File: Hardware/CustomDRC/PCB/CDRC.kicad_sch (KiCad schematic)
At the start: 1 part, among them J101 DSP Header

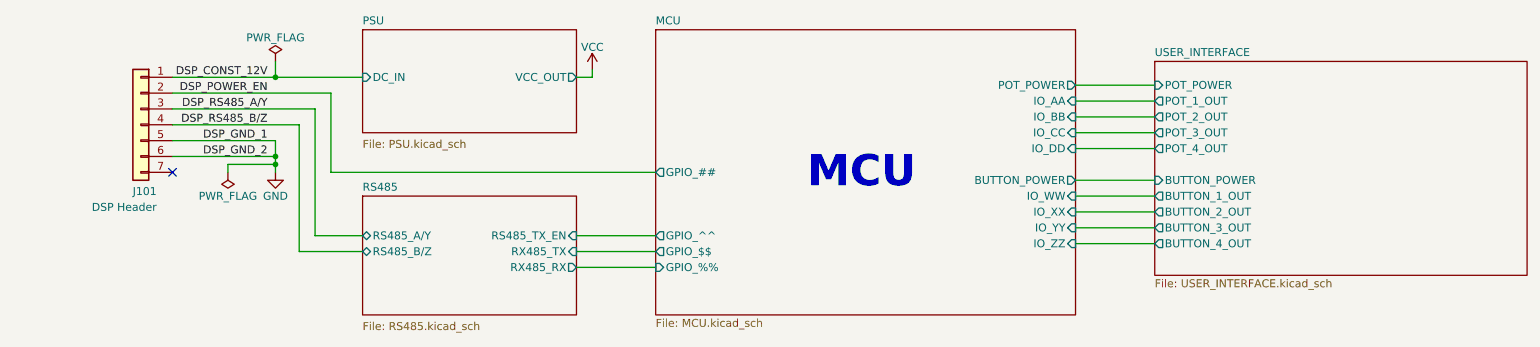
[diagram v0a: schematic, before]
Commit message: Update - Schematics
Added new reverse engineered schematic. Also updated main PCB folder structure
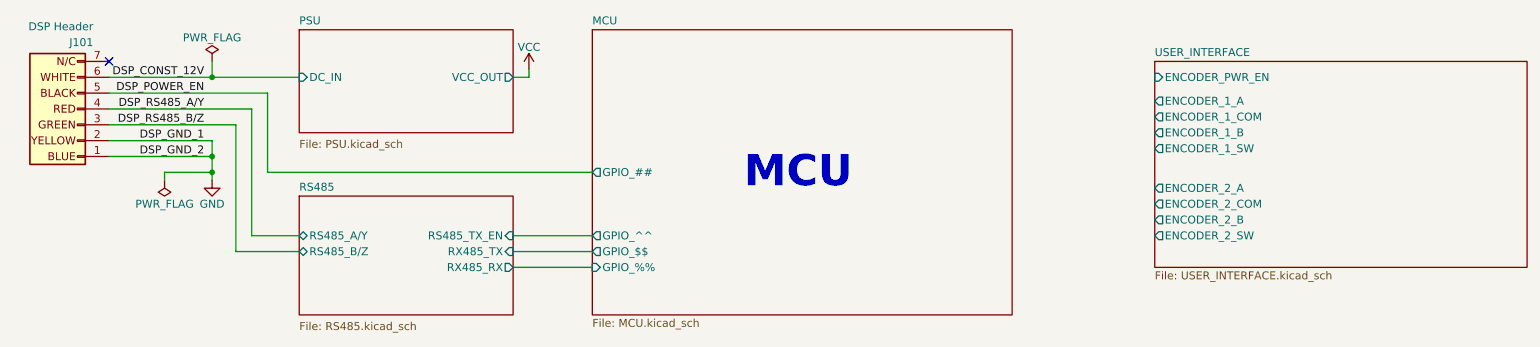
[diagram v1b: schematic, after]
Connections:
- net DSP_CONST_12V: now also J101.6 (Pin_6); no longer J101.1 (Pin_1)
- net DSP_POWER_EN: now also J101.5 (Pin_5); no longer J101.2 (Pin_2)
- net DSP_RS485_A/Y: now also J101.4 (Pin_4); no longer J101.3 (Pin_3)
- net DSP_RS485_B/Z: now also J101.3 (Pin_3); no longer J101.4 (Pin_4)
- net GND: now also J101.1 (Pin_1), J101.2 (Pin_2); no longer J101.5 (Pin_5), J101.6 (Pin_6)
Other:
- sheet MCU ports: added none; removed BUTTON_POWER, IO_AA, IO_BB, IO_CC, IO_DD, IO_WW, IO_XX, IO_YY, IO_ZZ, POT_POWER
- sheet USER_INTERFACE ports: added ENCODER_1_A, ENCODER_1_B, ENCODER_1_COM, ENCODER_1_SW, ENCODER_2_A, ENCODER_2_B, ENCODER_2_COM, ENCODER_2_SW, ENCODER_PWR_EN; removed BUTTON_1_OUT, BUTTON_2_OUT, BUTTON_3_OUT, BUTTON_4_OUT, BUTTON_POWER, POT_1_OUT, POT_2_OUT, POT_3_OUT, POT_4_OUT, POT_POWER

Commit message: Update - finished schematic for revision A
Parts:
- added H101, H102, H103: MountingHole, MountingHole:MountingHole_2.7mm_M2.5, symbol Mechanical:MountingHole
- added TP101: TestPoint_Small, TestPoint:TestPoint_Keystone_5000-5004_Miniature, symbol Connector:TestPoint_Small
- added TP102, TP103: TestPoint_Small, TestPoint:TestPoint_Pad_D1.5mm, symbol Connector:TestPoint_Small
- J101: LCSC (none) -> C18905866; MPN (none) -> XDZ254-1-06-W-2.5-G1; Manufacturer (none) -> chxunda
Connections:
- net DSP_CONST_12V: now also J101.7 (Pin_7), TP102.1; no longer J101.6 (Pin_6)
- net DSP_POWER_EN: now also J101.6 (Pin_6), TP103.1; no longer J101.5 (Pin_5)
- net DSP_RS485_A/Y: now also J101.5 (Pin_5); no longer J101.4 (Pin_4)
- net DSP_RS485_B/Z: now also J101.4 (Pin_4); no longer J101.3 (Pin_3)
- net GND: now also J101.3 (Pin_3), TP101.1; no longer J101.1 (Pin_1)
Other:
- sheet MCU ports: added GPIO36, GPIO39, IO18, IO19, IO21, IO25, IO32, IO33, IO34, IO35, IO5; removed GPIO_##, GPIO_$$, GPIO_%%, GPIO_^^
- sheet PSU ports: added none; removed VCC_OUT
- sheet RS485 ports: added RS485_RX, RS485_TX; removed RX485_RX, RX485_TX
- sheet USER_INTERFACE ports: added LED_PWM; removed ENCODER_1_COM, ENCODER_2_COM, ENCODER_PWR_EN
- moved on the sheet: J101

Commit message: Sync HW changes for V1 PCB
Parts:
- J101: LCSC C18905866 -> C7501615; MPN XDZ254-1-06-W-2.5-G1 -> PH2.54-07-06PWD; Manufacturer chxunda -> XUNPU
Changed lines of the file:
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@@
 	(title_block
 		(title "CDRC - Custom DRC for Audison AC Link")
-		(date "2024-08-20")
+		(date "03-09-2024")
 		(rev "A")
 		(company "JS HW")
@@
 			(width 0)
 			(type default)
+		)
+	)
+	(text_box "REVISION HISTORY:\n\nA: Initial design"
+		(exclude_from_sim no)
+		(at 177.546 139.7 0)
+		(size 101.6 20.828)
+		(stroke
+			(width 0)
+			(type default)
+		)
+		(fill
+			(type none)
+		)
+		(effects
+			(font
+				(size 2 2)
+				(thickness 0.4)
+				(bold yes)
+			)
+			(justify left top)
 		)
 	)
@@
 			)
 		)
-		(property "LCSC" " C18905866"
+		(property "LCSC" "C7501615"
 			(at 36.83 83.82 0)
 			(effects
@@
 			)
 		)
-		(property "Manufacturer" " chxunda"
+		(property "Manufacturer" "XUNPU"
 			(at 36.83 83.82 0)
 			(effects
@@
 			)
 		)
-		(property "MPN" "XDZ254-1-06-W-2.5-G1"
+		(property "MPN" "PH2.54-07-06PWD"
 			(at 36.83 83.82 0)
 			(effects

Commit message: Sync before making breaking changes to RS485 comms protocl and method
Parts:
- H101, H102, H103: footprint MountingHole:MountingHole_2.7mm_M2.5 -> MountingHole:MountingHole_2.7mm_M2.5_ISO7380_Pad_TopOnly
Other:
- sheet MCU ports: added IO27, IO36, IO39; removed GPIO36, GPIO39, IO21
- title: CDRC - Custom DRC for Audison AC Link -> CDRC - Custom DRC for Bit 10D
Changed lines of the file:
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@@
 	(paper "A4")
 	(title_block
-		(title "CDRC - Custom DRC for Audison AC Link")
-		(date "03-09-2024")
-		(rev "A")
+		(title "CDRC - Custom DRC for Bit 10D")
+		(date "01-11-2024")
+		(rev "B")
 		(company "JS HW")
 	)
@@
 		)
 	)
-	(text_box "REVISION HISTORY:\n\nA: Initial design"
+	(text_box "ISSUES:\n- DRC requires listenting to RS485 on sleep to wake-up when DSP is powered on.\n	Requires ESP32 to assign RX pin to an RTC power domain IO (IO27 will work)"
+		(exclude_from_sim no)
+		(at 18.796 164.338 0)
+		(size 101.092 28.702)
+		(stroke
+			(width 0)
+			(type default)
+		)
+		(fill
+			(type none)
+		)
+		(effects
+			(font
+				(size 1.27 1.27)
+				(thickness 0.254)
+				(bold yes)
+			)
+			(justify left top)
+		)
+	)
+	(text_box "REVISION HISTORY:\n\nA: Initial design\nB: Changed RS485 RX connection to ESP32 from GPIO21 to GPIO27	\nRemoved solder bridge pads to control RS485_RX_EN. Confirmed working as intended"
 		(exclude_from_sim no)
 		(at 177.546 139.7 0)
-		(size 101.6 20.828)
+		(size 101.6 24.892)
 		(stroke
 			(width 0)
@@
 			)
 		)
-		(property "Footprint" "MountingHole:MountingHole_2.7mm_M2.5"
+		(property "Footprint" "MountingHole:MountingHole_2.7mm_M2.5_ISO7380_Pad_TopOnly"
 			(at 96.52 135.89 0)
 			(effects
@@
 			)
 		)
-		(property "Footprint" "MountingHole:MountingHole_2.7mm_M2.5"
+		(property "Footprint" "MountingHole:MountingHole_2.7mm_M2.5_ISO7380_Pad_TopOnly"
 			(at 96.52 148.59 0)
 			(effects
@@
 			)
 		)
-		(property "Footprint" "MountingHole:MountingHole_2.7mm_M2.5"
+		(property "Footprint" "MountingHole:MountingHole_2.7mm_M2.5_ISO7380_Pad_TopOnly"
 			(at 96.52 142.24 0)
 			(effects
@@
 			)
 		)
-		(pin "GPIO39" input
-			(at 186.69 91.44 0)
-			(effects
-				(font
-					(size 1.27 1.27)
-				)
-				(justify right)
-			)
-		)
-		(pin "GPIO36" input
-			(at 186.69 88.9 0)
-			(effects
-				(font
-					(size 1.27 1.27)
-				)
-				(justify right)
-			)
-		)
 		(pin "IO19" bidirectional
 			(at 119.38 101.6 180)
@@
 			)
 		)
-		(pin "IO21" bidirectional
-			(at 119.38 106.68 180)
-			(effects
-				(font
-					(size 1.27 1.27)
-				)
-				(justify left)
-			)
-		)
 		(pin "IO5" output
 			(at 119.38 91.44 180)
 			(effects
 				(font
+					(size 1.27 1.27)
+				)
+				(justify left)
+			)
+		)
+		(pin "IO36" input
+			(at 186.69 88.9 0)
+			(effects
+				(font
+					(size 1.27 1.27)
+				)
+				(justify right)
+			)
+		)
+		(pin "IO39" input
+			(at 186.69 91.44 0)
+			(effects
+				(font
+					(size 1.27 1.27)
+				)
+				(justify right)
+			)
+		)
+		(pin "IO27" bidirectional
+			(at 119.38 106.68 180)
+			(effects
+				(font

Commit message: Sync changes to Rev B HW
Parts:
- added H104: MountingHole, MountingHole:MountingHole_2.7mm_M2.5_ISO7380_Pad_TopBottom, symbol Mechanical:MountingHole
- H101, H102, H103: footprint MountingHole:MountingHole_2.7mm_M2.5_ISO7380_Pad_TopOnly -> MountingHole:MountingHole_2.7mm_M2.5_ISO7380_Pad_TopBottom
- J101: footprint Connector_PinHeader_2.54mm:PinHeader_1x07_P2.54mm_Horizontal -> CDRC_Footprints:M208900705; LCSC C7501615 -> C20610239; MPN PH2.54-07-06PWD -> KH-2.54PH-1X30P-L13.5-WT; Manufacturer XUNPU -> Shenzhen Kinghelm Elec; Note (none) -> Bulk amount of connector pins, can separate and then solder
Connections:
- net DSP_CONST_12V: now also J101.1 (Pin_1); no longer J101.7 (Pin_7)
- net DSP_POWER_EN: now also J101.2 (Pin_2); no longer J101.6 (Pin_6)
- net DSP_RS485_A/Y: now also J101.3 (Pin_3); no longer J101.5 (Pin_5)
- net GND: now also J101.5 (Pin_5), J101.6 (Pin_6); no longer J101.2 (Pin_2), J101.3 (Pin_3)
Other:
- moved on the sheet: H101, H102, H103, J101, TP101, TP102, TP103

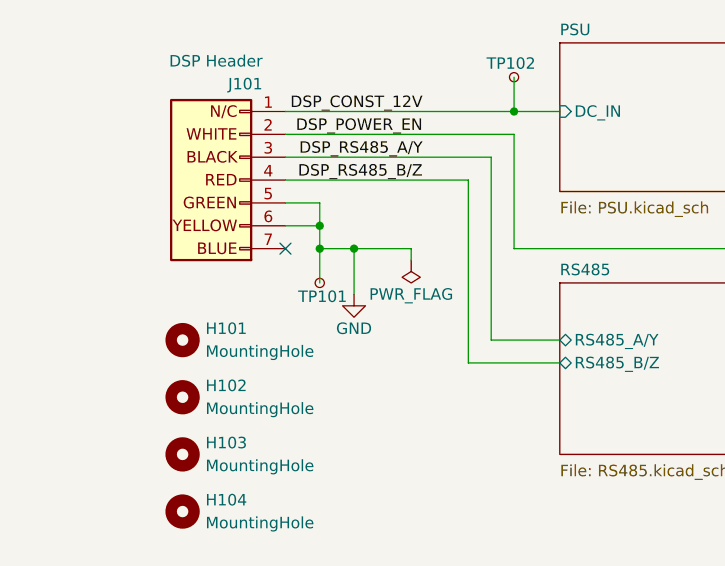
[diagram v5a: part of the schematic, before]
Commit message: Added board renders and PDF plots
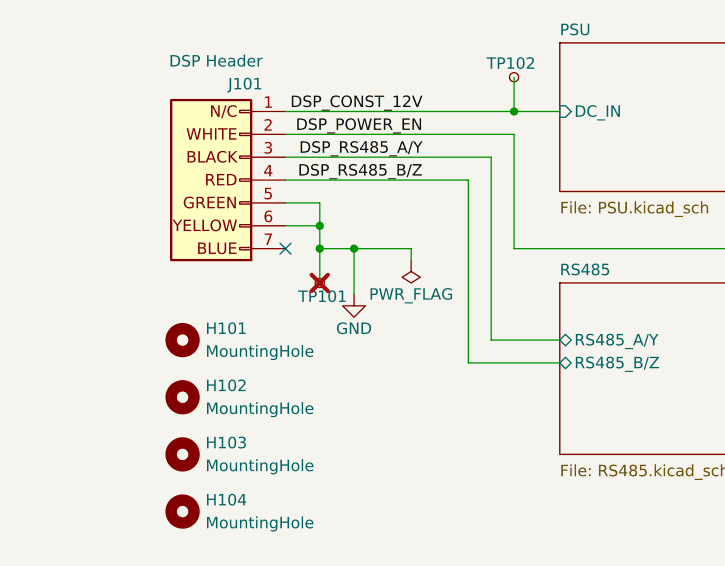
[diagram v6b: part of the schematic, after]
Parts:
- TP101: now not fitted; now left out of the parts list
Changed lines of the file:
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@@
 		(unit 1)
 		(exclude_from_sim no)
-		(in_bom yes)
+		(in_bom no)
 		(on_board yes)
-		(dnp no)
+		(dnp yes)
 		(property "Reference" "TP101"
 			(at 51.308 72.644 0)
